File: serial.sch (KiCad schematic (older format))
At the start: 53 parts, among them CN304 Conn_02x13_Odd_Even, CN305 DB25P, CN306 Conn_01x03_Male, Q300 2SC945, Q302 2N3906, U301 8520, U302 74LS32, U303 74F08, U304 1488, U305 1489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

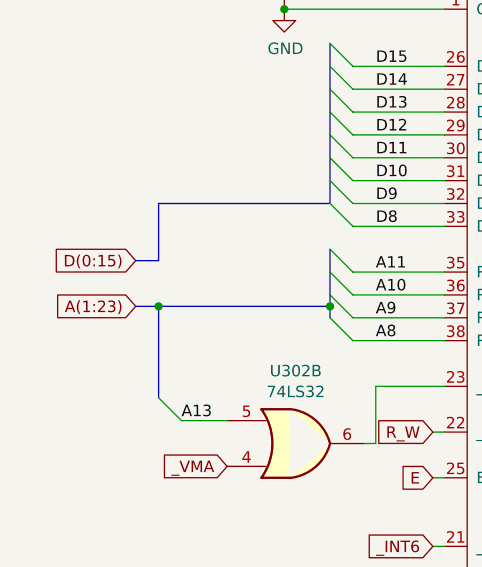
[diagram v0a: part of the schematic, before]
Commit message: Rename bus with correct syntax
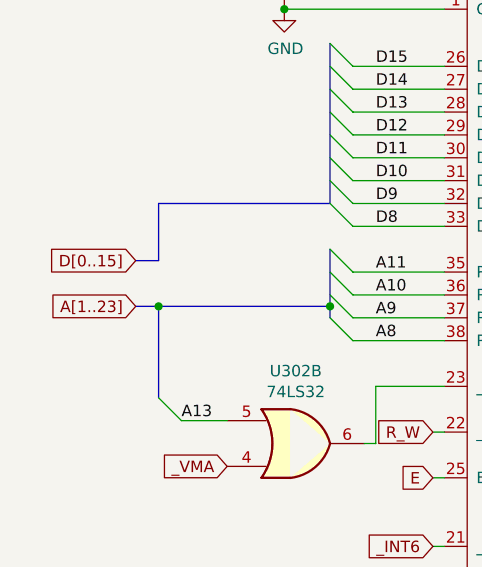
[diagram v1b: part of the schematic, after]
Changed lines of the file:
@@
-EESchema Schematic File Version 4
+EESchema Schematic File Version 5
 LIBS:amiga2000-cache
 EELAYER 29 0
@@
 A13
 Text GLabel 950  5700 0    50   Input ~ 0
-D(0:15)
+D[0..15]
 Text GLabel 950  5900 0    50   Input ~ 0
-A(1:23)
+A[1..23]
 Wire Wire Line
 	1350 6400 1150 6400

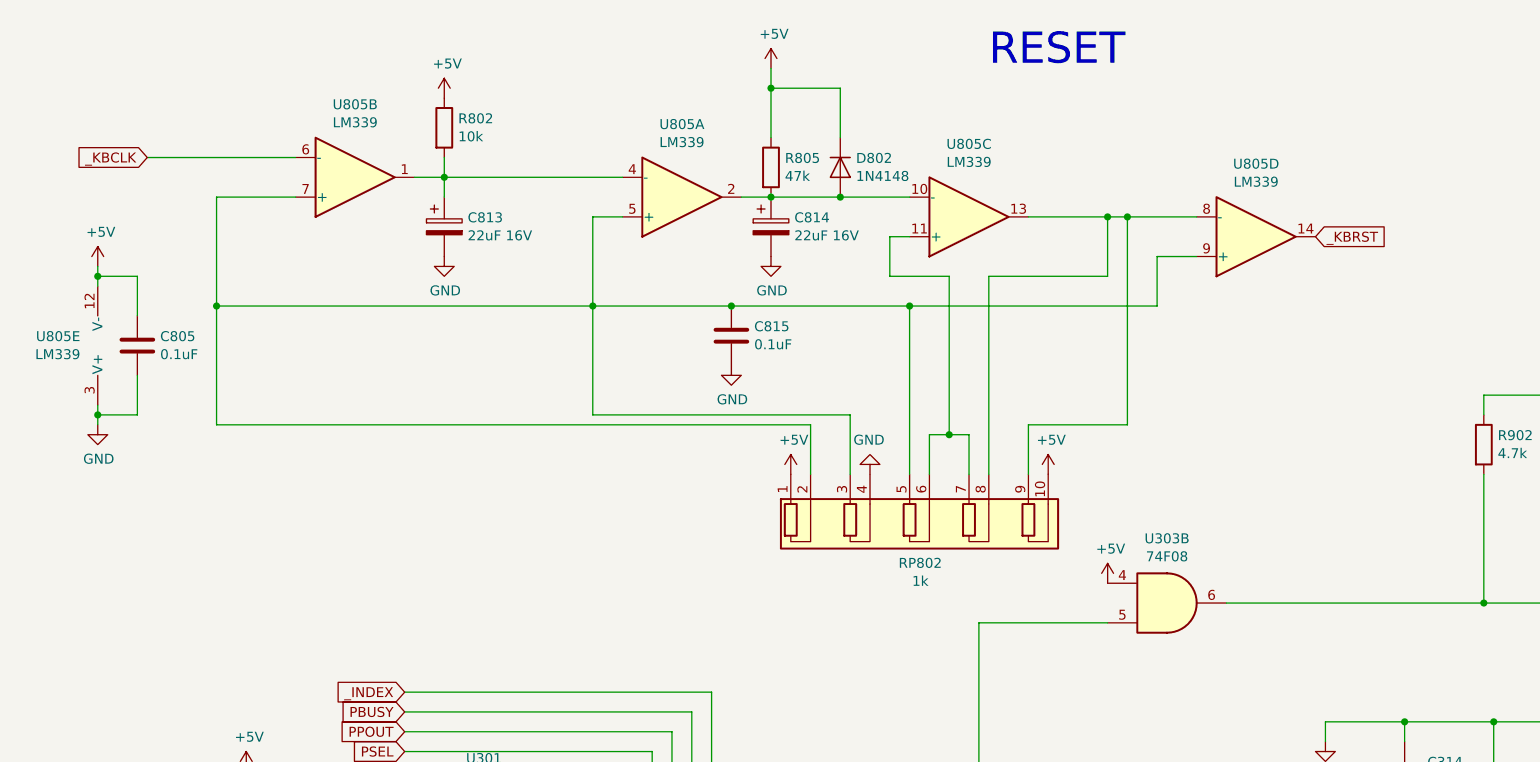
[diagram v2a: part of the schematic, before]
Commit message: Implemented various rev 6.2 fixes from forums and my own board
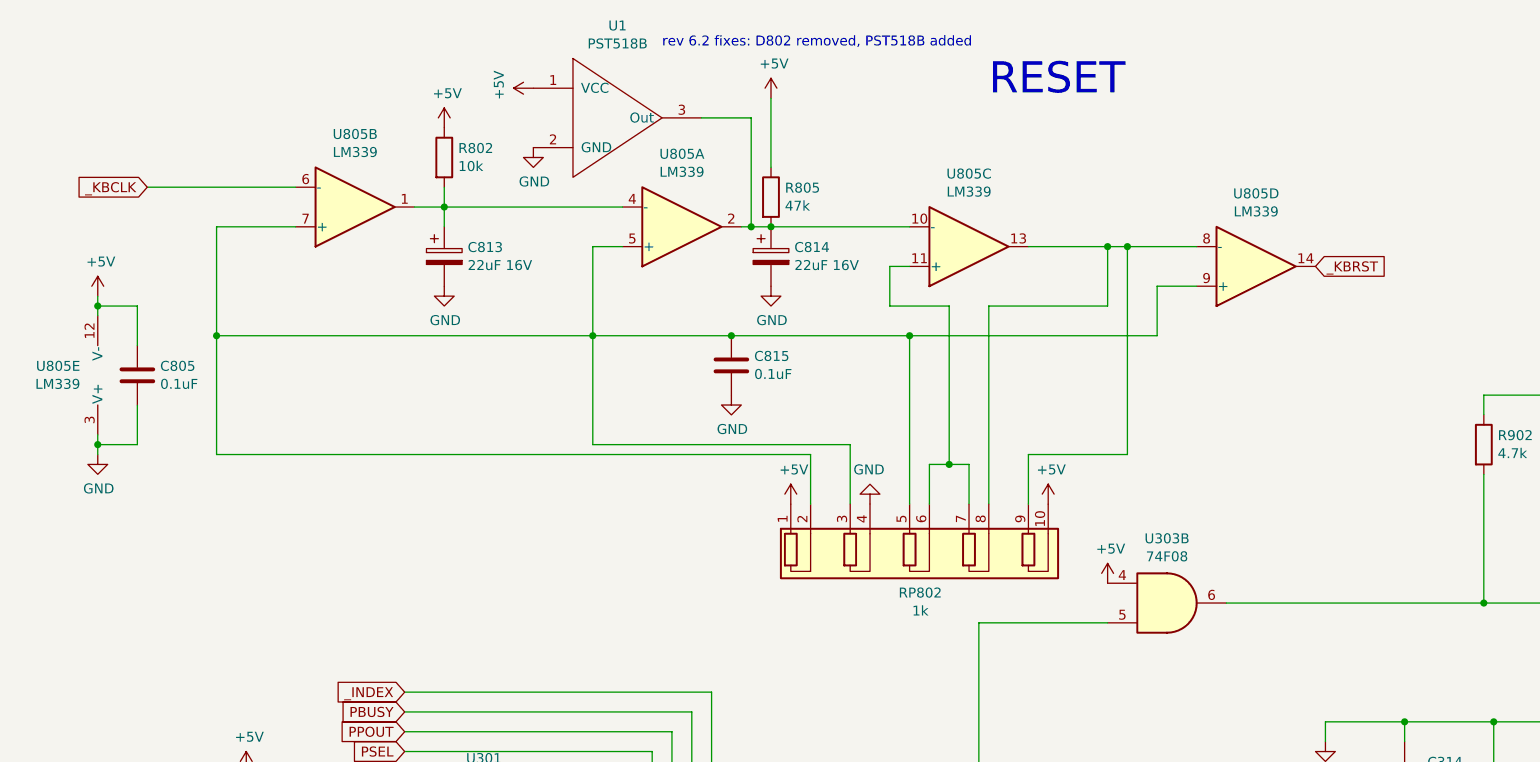
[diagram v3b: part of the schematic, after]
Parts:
- removed D802: 1N4148, Diode_THT:D_DO-35_SOD27_P7.62mm_Horizontal, symbol Diode:1N4148
- added U1: PST518B, symbol d_ics:PST518B
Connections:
- net +5V: now also U1.1 (VCC)
- net GND: now also U1.2 (GND)
- net at C814.1, R805.2, U805.10 (-)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: now also U1.3 (Out)
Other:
- note added: "rev 6.2 fixes: D802 removed, PST518B added"
- moved on the sheet: C805, C813, C814, C815, R802, R805, RP802, U805A, U805B, U805C, U805D, U805E

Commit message: Bump rev, update readme
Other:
- note added: "rev 6.2 fixes: D802 removed, PST518B added\nalso that makes the ERC cry but whatever..."
- note removed: "rev 6.2 fixes: D802 removed, PST518B added"
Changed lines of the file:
@@
 Title "B2000 Serial and Reset"
 Date "07/06/1987"
-Rev "6.0-1"
+Rev "6.2-a"
 Comp "Commodore"
 Comment1 "Drawn by: Dave Haynie"
@@
 L power:+5V #PWR040
 U 1 1 5DC95AE9
-P 4250 900
-F 0 "#PWR040" H 4250 750 50  0001 C CNN
-F 1 "+5V" H 4265 1073 50  0000 C CNN
-F 2 "" H 4250 900 50  0001 C CNN
-F 3 "" H 4250 900 50  0001 C CNN
-	1    4250 900
+P 4250 1100
+F 0 "#PWR040" H 4250 950 50  0001 C CNN
+F 1 "+5V" H 4265 1273 50  0000 C CNN
+F 2 "" H 4250 1100 50  0001 C CNN
+F 3 "" H 4250 1100 50  0001 C CNN
+	1    4250 1100
 	1    0    0    -1
 $EndComp
@@
 Text GLabel 7000 1750 2    50   Input ~ 0
 _KBRST
-Text Notes 5350 900  0    157  ~ 0
+Text Notes 5700 1050 0    157  ~ 0
 RESET
 Wire Wire Line
@@
 	4250 1550 4950 1550
 Wire Wire Line
-	4250 900  4250 1250
-Text Notes 3700 650  0    50   ~ 0
-rev 6.2 fixes: D802 removed, PST518B added
+	4250 1100 4250 1250
 $Comp
 L power:+5V #PWR0263
@@
 Wire Wire Line
 	4150 1000 4150 1550
+Connection ~ 4150 1550
+Wire Wire Line
+	4150 1550 4250 1550
 Wire Bus Line
 	1800 5650 1800 5900
 Wire Bus Line
 	1800 4750 1800 5450
-Connection ~ 4150 1550
-Wire Wire Line
-	4150 1550 4250 1550
+Text Notes 3750 750  0    50   ~ 0
+rev 6.2 fixes: D802 removed, PST518B added\nalso that makes the ERC cry but whatever...
 $EndSCHEMATC

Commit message: Add gender to connectors
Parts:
- CN304: Gender (none) -> Male
- CN305: symbol Connector:DB25_Female -> Connector:DB25_Male_MountingHoles; Gender (none) -> Male
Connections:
- net GND: now also CN305.0 (PAD)
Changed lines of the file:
@@
 Connection ~ 5150 2750
 $Comp
-L Connector:DB25_Female CN305
+L Connector:DB25_Male_MountingHoles CN305
 U 1 1 5DD269D4
 P 14650 6650
@@
 F 2 "" H 14650 6650 50  0001 C CNN
 F 3 " ~" H 14650 6650 50  0001 C CNN
+F 4 "Male" H 14650 6650 50  0001 C CNN "Gender"
 	1    14650 6650
-	1    0    0    -1
+	1    0    0    1
 $EndComp
 $Comp
@@
 F 2 "" H 11050 4200 50  0001 C CNN
 F 3 "~" H 11050 4200 50  0001 C CNN
+F 4 "Male" V 11050 4200 50  0001 C CNN "Gender"
 	1    11050 4200
 	0    -1   -1   0
@@
 	1    0    0    -1
 $EndComp
-Text Notes 13750 5200 0    157  ~ 0
+Text Notes 13800 5050 0    157  ~ 0
 EXTERNAL SERIAL
 $Comp
@@
 Wire Bus Line
 	1800 4750 1800 5450
+$Comp
+L power:GND #PWR?
+U 1 1 5D8F7764
+P 14650 5250
+F 0 "#PWR?" H 14650 5000 50  0001 C CNN
+F 1 "GND" H 14655 5077 50  0000 C CNN
+F 2 "" H 14650 5250 50  0001 C CNN
+F 3 "" H 14650 5250 50  0001 C CNN
+	1    14650 5250
+	0    -1   -1   0
+$EndComp
 $EndSCHEMATC
